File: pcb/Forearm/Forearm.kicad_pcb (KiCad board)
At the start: 4 copper layers, 64 x 64.1 mm, 22 parts, among them J1 Conn_01x02, J2 Conn_01x16_Top, J3 Conn_01x16_Bottom, J9 Conn_01x01, U1 ESP32-S3-DEVKITC-1-N8R2, U2 4754

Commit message: actually final pcbs
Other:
- board text added: "Dexterity Forearm JLL"
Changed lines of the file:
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@@
 		(property "Reference" "C1"
 			(at -3.253 0 180)
+			(unlocked yes)
 			(layer "F.SilkS")
 			(effects
 				(font
-					(size 1 1)
-					(thickness 0.15)
+					(size 1.016 1.016)
+					(thickness 0.1524)
 				)
 			)
@@
 		(property "Reference" "J9"
 			(at -0.0254 2.4892 0)
+			(unlocked yes)
 			(layer "F.SilkS")
 			(effects
 				(font
-					(size 1 1)
-					(thickness 0.15)
+					(size 1.016 1.016)
+					(thickness 0.1524)
 				)
 			)
@@
 		(property "Reference" "U1"
 			(at -14.224 -28.9032 0)
+			(unlocked yes)
 			(layer "F.SilkS")
 			(effects
 				(font
-					(size 1 1)
-					(thickness 0.15)
+					(size 1.016 1.016)
+					(thickness 0.1524)
 				)
 			)
@@
 		(property "Reference" "VR1"
 			(at -6.604 -2.032 -90)
+			(unlocked yes)
 			(layer "F.SilkS")
 			(effects
 				(font
-					(size 1.4 1.4)
-					(thickness 0.15)
+					(size 1.016 1.016)
+					(thickness 0.1524)
 				)
 			)
@@
 		(property "Reference" "REF**"
 			(at 0 -3.2 0)
+			(unlocked yes)
 			(layer "F.SilkS")
 			(hide yes)
 			(effects
 				(font
-					(size 1 1)
-					(thickness 0.15)
+					(size 1.016 1.016)
+					(thickness 0.1524)
 				)
 			)
@@
 		(property "Reference" "J1"
 			(at 0 -2.77 90)
+			(unlocked yes)
 			(layer "F.SilkS")
 			(effects
 				(font
-					(size 1 1)
-					(thickness 0.15)
+					(size 1.016 1.016)
+					(thickness 0.1524)
 				)
 			)
@@
 		(property "Reference" "U2"
 			(at 12.319 -12.573 0)
+			(unlocked yes)
 			(layer "F.SilkS")
 			(effects
 				(font
-					(size 1 1)
-					(thickness 0.15)
+					(size 1.016 1.016)
+					(thickness 0.1524)
 				)
 			)
@@
 		(property "Reference" "C2"
 			(at -3.302 0 180)
+			(unlocked yes)
 			(layer "F.SilkS")
 			(effects
 				(font
-					(size 1 1)
-					(thickness 0.15)
+					(size 1.016 1.016)
+					(thickness 0.1524)
 				)
 			)
@@
 		(property "Reference" "REF**"
 			(at 0 -3.2 0)
+			(unlocked yes)
 			(layer "F.SilkS")
 			(hide yes)
 			(effects
 				(font
-					(size 1 1)
-					(thickness 0.15)
+					(size 1.016 1.016)
+					(thickness 0.1524)
 				)
 			)
@@
 		(property "Reference" "REF**"
 			(at 0 -3.2 0)
+			(unlocked yes)
 			(layer "F.SilkS")
 			(hide yes)
 			(effects
 				(font
-					(size 1 1)
-					(thickness 0.15)
+					(size 1.016 1.016)
+					(thickness 0.1524)
 				)
 			)
@@
 		(tags "522071633 ")
 		(property "Reference" "J2"
-			(at 0 -7.62 180)
+			(at -0.547985 0.406001 180)
 			(unlocked yes)
 			(layer "F.SilkS")
 			(effects
 				(font
-					(size 1 1)
-					(thickness 0.15)
+					(size 1.016 1.016)
+					(thickness 0.1524)
 				)
 			)
@@
 			(at 0 -10.16 180)
 			(unlocked yes)
-			(layer "F.SilkS")
-			(effects
-				(font
-					(size 1 1)
-					(thickness 0.15)
-				)
-			)
-		)
-		(fp_text user "522071633"
-			(at 0 -10.16 180)
-			(unlocked yes)
 			(layer "F.Fab")
 			(effects
@@
 		(property "Reference" "RS0"
 			(at 0 1.17 90)
+			(unlocked yes)
 			(layer "B.SilkS")
 			(effects
 				(font
-					(size 1 1)
-					(thickness 0.15)
+					(size 1.016 1.016)
+					(thickness 0.1524)
 				)
 				(justify mirror)
@@
 		(property "Reference" "B0"
 			(at 0 2.77 90)
+			(unlocked yes)
 			(layer "B.SilkS")
 			(effects
 				(font
-					(size 1 1)
-					(thickness 0.15)
+					(size 1.016 1.016)
+					(thickness 0.1524)
 				)
 				(justify mirror)
@@
 		(property "Reference" "RLED0"
 			(at 0 1.17 0)
+			(unlocked yes)
 			(layer "B.SilkS")
 			(effects
 				(font
-					(size 1 1)
-					(thickness 0.15)
+					(size 1.016 1.016)
+					(thickness 0.1524)
 				)
 				(justify mirror)
@@
 		(property "Reference" "LED1"
 			(at 0 2.77 90)
+			(unlocked yes)
 			(layer "B.SilkS")
 			(effects
 				(font
-					(size 1 1)
-					(thickness 0.15)
+					(size 1.016 1.016)
+					(thickness 0.1524)
 				)
 				(justify mirror)
@@
 		(tags "522071633 ")
 		(property "Reference" "J3"
-			(at 0 7.62 180)
+			(at 0.293985 -0.406001 180)
 			(unlocked yes)
 			(layer "B.SilkS")
 			(effects
 				(font
-					(size 1 1)
-					(thickness 0.15)
+					(size 1.016 1.016)
+					(thickness 0.1524)
 				)
 				(justify mirror)
@@
 			(at 0 10.16 180)
 			(unlocked yes)
-			(layer "B.SilkS")
-			(effects
-				(font
-					(size 1 1)
-					(thickness 0.15)
-				)
-				(justify mirror)
-			)
-		)
-		(fp_text user "522071633"
-			(at 0 10.16 180)
-			(unlocked yes)
 			(layer "B.Fab")
 			(effects
@@
 		(property "Reference" "RB0"
 			(at 0 1.17 90)
+			(unlocked yes)
 			(layer "B.SilkS")
 			(effects
 				(font
-					(size 1 1)
-					(thickness 0.15)
+					(size 1.016 1.016)
+					(thickness 0.1524)
 				)
 				(justify mirror)
@@
 		(property "Reference" "LED0"
 			(at 0 2.77 90)
+			(unlocked yes)
 			(layer "B.SilkS")
 			(effects
 				(font
-					(size 1 1)
-					(thickness 0.15)
+					(size 1.016 1.016)
+					(thickness 0.1524)
 				)
 				(justify mirror)
@@
 		(property "Reference" "RLED1"
 			(at 0 1.17 0)
+			(unlocked yes)
 			(layer "B.SilkS")
 			(effects
 				(font
-					(size 1 1)
-					(thickness 0.15)
+					(size 1.016 1.016)
+					(thickness 0.1524)
 				)
 				(justify mirror)
@@
 		(property "Reference" "S0"
 			(at 0 2.77 90)
+			(unlocked yes)
 			(layer "B.SilkS")
 			(effects
 				(font
-					(size 1 1)
-					(thickness 0.15)
+					(size 1.016 1.016)
+					(thickness 0.1524)
 				)
 				(justify mirror)
@@
 		(property "Reference" "RB1"
 			(at 0 1.17 90)
+			(unlocked yes)
 			(layer "B.SilkS")
 			(effects
 				(font
-					(size 1 1)
-					(thickness 0.15)
+					(size 1.016 1.016)
+					(thickness 0.1524)
 				)
 				(justify mirror)
@@
 		(property "Reference" "B1"
 			(at 0 2.77 90)
+			(unlocked yes)
 			(layer "B.SilkS")
 			(effects
 				(font
-					(size 1 1)
-					(thickness 0.15)
+					(size 1.016 1.016)
+					(thickness 0.1524)
 				)
 				(justify mirror)
@@
 		(layer "Edge.Cuts")
 	)
+	(gr_text "Dexterity\nForearm\nJLL"
+		(at 21.7536 81.3928 0)
+		(layer "F.SilkS")
+		(effects
+			(font
+				(size 1.016 1.016)
+				(thickness 0.1524)
+			)
+			(justify bottom)
+		)
+	)
 	(segment

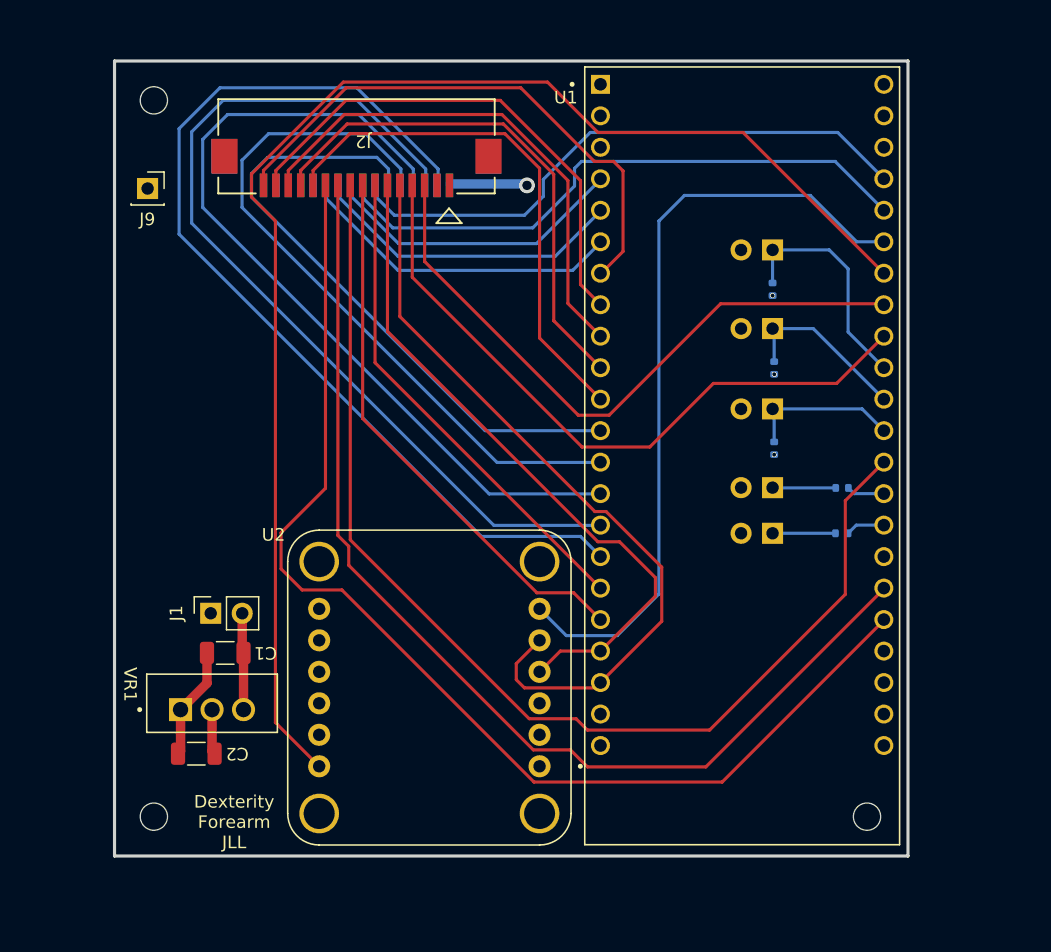
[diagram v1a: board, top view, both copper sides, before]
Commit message: added ground pours and generated gerbers for pcbs
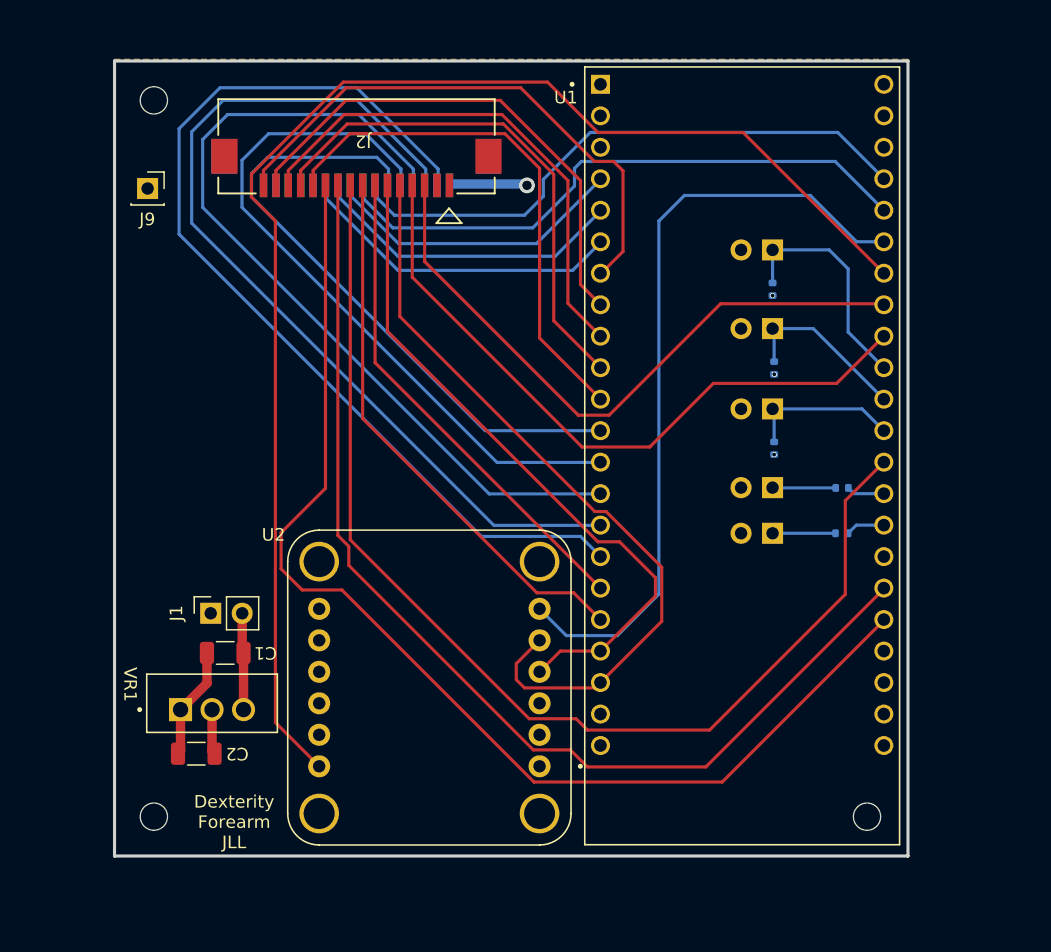
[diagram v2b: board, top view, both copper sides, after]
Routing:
- added copper zone on B.Cu, net GND
- added copper zone on F.Cu, net GND
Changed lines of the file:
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@@
 		(grid_origin 12.1016 81.9008)
 		(pcbplotparams
-			(layerselection 0x00010f0_ffffffff)
+			(layerselection 0x00010fc_ffffffff)
 			(plot_on_all_layers_selection 0x0000000_00000000)
 			(disableapertmacros no)
-			(usegerberextensions no)
-			(usegerberattributes yes)
-			(usegerberadvancedattributes yes)
-			(creategerberjobfile yes)
+			(usegerberextensions yes)
+			(usegerberattributes no)
+			(usegerberadvancedattributes no)
+			(creategerberjobfile no)
 			(dashed_line_dash_ratio 12.000000)
 			(dashed_line_gap_ratio 3.000000)
@@
 			(plotinvisibletext no)
 			(sketchpadsonfab no)
-			(subtractmaskfromsilk no)
+			(subtractmaskfromsilk yes)
 			(outputformat 1)
 			(mirror no)
@@
 	)
 	(zone
+		(net 1)
+		(net_name "GND")
+		(layer "F.Cu")
+		(hatch edge 0.5)
+		(priority 2)
+		(connect_pads
+			(clearance 0.5)
+		)
+		(min_thickness 0.25)
+		(filled_areas_thickness no)
+		(fill yes
+			(thermal_gap 0.5)
+			(thermal_bridge_width 0.5)
+		)
+		(polygon
+			(pts
+				(xy 12.1016 17.6388) (xy 76.1096 17.6388) (xy 76.1096 81.9008) (xy 12.1016 81.9008)
+			)
+		)
+	)
+	(zone
 		(net 3)
 		(net_name "3V3")
@@
 			)
 		)
+	)
+	(zone
+		(net 1)
+		(net_name "GND")
+		(layer "B.Cu")
+		(hatch edge 0.5)
+		(priority 3)
+		(connect_pads
+			(clearance 0.5)
+		)
+		(min_thickness 0.25)
+		(filled_areas_thickness no)
+		(fill yes
+			(thermal_gap 0.5)
+			(thermal_bridge_width 0.5)
+		)
+		(polygon
+			(pts
+				(xy 76.1096 17.6388) (xy 76.1096 81.9008) (xy 12.1016 81.9008) (xy 12.1016 17.6388)
+			)
+		)

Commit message: edited esp32 footprint
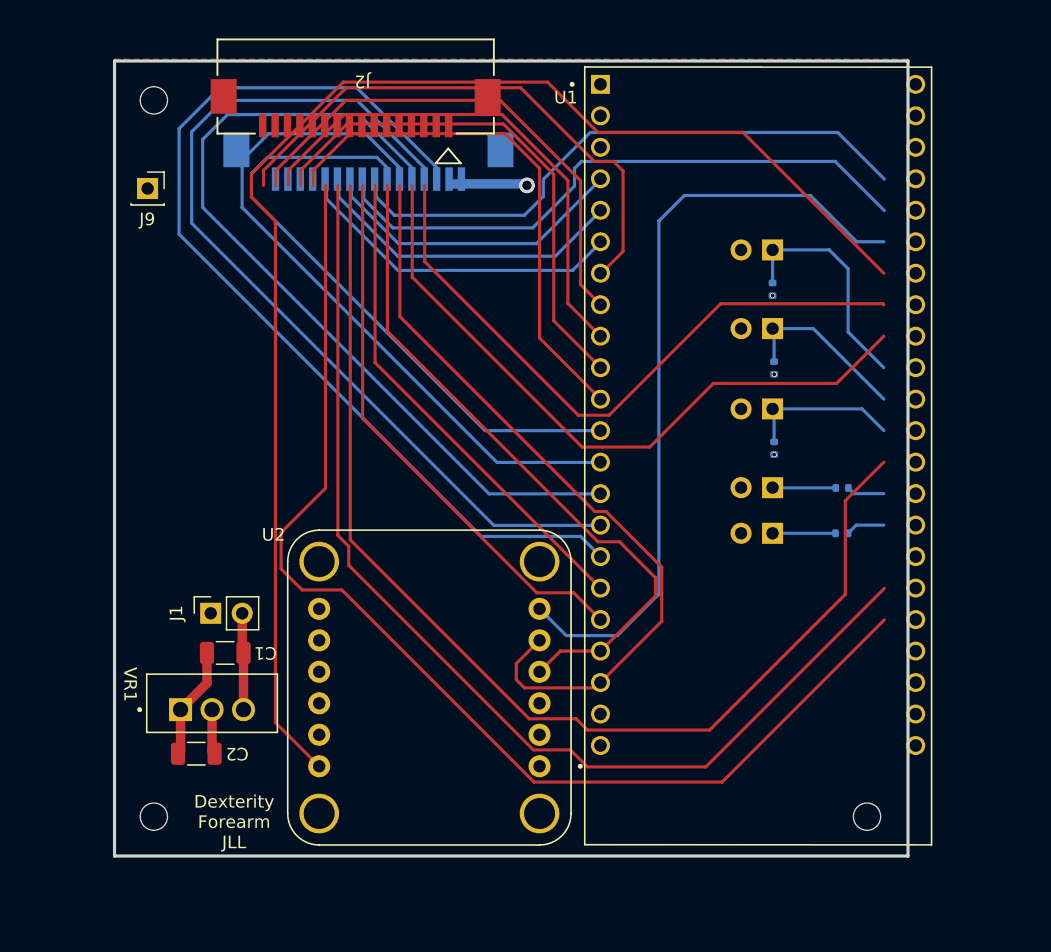
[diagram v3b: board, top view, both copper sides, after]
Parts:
- moved J2 4.83 mm to (31.6, 19.8)
- moved J3 1.09 mm to (32.6, 24.1)
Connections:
- J2 pad 1: unconnected-(J2-Pin_1-Pad1) -> FEEDBACK_D4
- J2 pad 10: HAPTIC_S1 -> HAPTIC_SCL
- J2 pad 11: HAPTIC_S0 -> IMU_SCL
- J2 pad 12: FEEDBACK_D0 -> IMU_SDA
- J2 pad 13: FEEDBACK_D1 -> IMU_1_RST
- J2 pad 14: FEEDBACK_D2 -> IMU_1_INT
- J2 pad 15: FEEDBACK_D3 -> unconnected-(J2-Pin_15-Pad15)
- J2 pad 16: FEEDBACK_D4 -> unconnected-(J2-Pin_16-Pad16)
- J2 pad 2: unconnected-(J2-Pin_2-Pad2) -> FEEDBACK_D3
- J2 pad 3: IMU_1_INT -> FEEDBACK_D2
- J2 pad 4: IMU_1_RST -> FEEDBACK_D1
- J2 pad 5: IMU_SDA -> FEEDBACK_D0
- J2 pad 6: IMU_SCL -> HAPTIC_S0
- J2 pad 7: HAPTIC_SCL -> HAPTIC_S1
- J2 pad 8: HAPTIC_SDA -> HAPTIC_S2
- J2 pad 9: HAPTIC_S2 -> HAPTIC_SDA
- J3 pad 1: unconnected-(J3-Pin_1-Pad1) -> 3V3
- J3 pad 10: SPOOLPOT_ADC0 -> SPOOLPOT_ADC3
- J3 pad 11: HALL_S3 -> SPOOLPOT_ADC4
- J3 pad 12: HALL_S2 -> GND
- J3 pad 13: HALL_S1 -> unconnected-(J3-Pin_13-Pad13)
- J3 pad 14: HALL_S0 -> unconnected-(J3-Pin_14-Pad14)
- J3 pad 15: HALL_ADC -> unconnected-(J3-Pin_15-Pad15)
- J3 pad 16: 3V3 -> unconnected-(J3-Pin_16-Pad16)
- J3 pad 2: unconnected-(J3-Pin_2-Pad2) -> HALL_ADC
- J3 pad 3: unconnected-(J3-Pin_3-Pad3) -> HALL_S0
- J3 pad 4: unconnected-(J3-Pin_4-Pad4) -> HALL_S1
- J3 pad 5: unconnected-(J3-Pin_5-Pad5) -> HALL_S2
- J3 pad 6: SPOOLPOT_ADC4 -> HALL_S3
- J3 pad 7: SPOOLPOT_ADC3 -> SPOOLPOT_ADC0
- J3 pad 8: SPOOLPOT_ADC2 -> SPOOLPOT_ADC1
- J3 pad 9: SPOOLPOT_ADC1 -> SPOOLPOT_ADC2
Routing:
- net SPOOLPOT_ADC2: track 24.9 -> 72.7 mm
- net SPOOLPOT_ADC0: track 47.8 -> 0.00 mm
- net unconnected-(J3-Pin_16-Pad16): track 0.00 -> 6.22 mm
- net 3V3: track 9.86 -> 3.64 mm

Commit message: updated esp32 pins on schematic
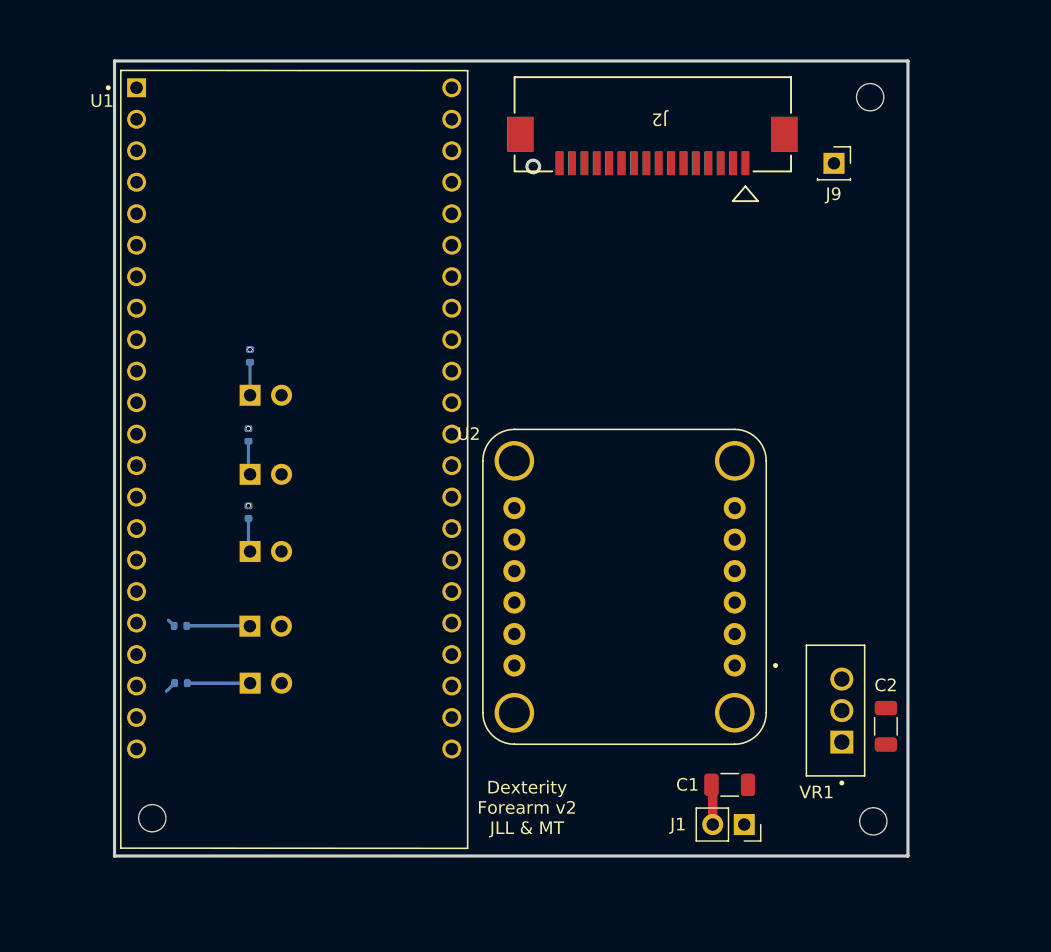
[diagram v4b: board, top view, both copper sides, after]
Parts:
- moved REF** 57.8 mm to (73.1, 20.7)
- moved C2 55.7 mm to (74.3, 71.4), turned to -90 degrees
- moved J9 55.4 mm to (70.1, 26.0)
- moved RLED1 54.7 mm to (17.5, 68.0), turned to 180 degrees
- moved RLED0 54.5 mm to (17.4, 63.3), turned to 180 degrees
- moved VR1 50.8 mm to (70.8, 70.2), turned to 90 degrees
- moved J1 46.3 mm to (62.9, 79.4), turned to -90 degrees
- moved LED1 43.8 mm to (23.0, 68.0), turned to -90 degrees
- moved B0 43.8 mm to (23.0, 51.1), turned to -90 degrees
- moved S0 43.8 mm to (23.0, 44.7), turned to -90 degrees
- moved B1 43.7 mm to (23.0, 57.3), turned to -90 degrees
- moved LED0 43.6 mm to (23.0, 63.4), turned to -90 degrees
- moved RB0 42.7 mm to (22.9, 47.9), turned to 90 degrees
- moved RB1 42.7 mm to (22.9, 54.2), turned to 90 degrees
- moved RS0 42.5 mm to (23.0, 41.6), turned to 90 degrees
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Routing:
- net IMU_0_RST: track 110.5 -> 0.00 mm
- net HAPTIC_S0: track 93.6 -> 0.00 mm
- net HAPTIC_S2: track 91.4 -> 0.00 mm
- net HAPTIC_S1: track 86.9 -> 0.00 mm
- net HALL_ADC: track 79.5 -> 0.00 mm
- net HALL_S0: track 73.9 -> 0.00 mm
- net SPOOLPOT_ADC2: track 72.7 -> 0.00 mm
- net HALL_S1: track 68.0 -> 0.00 mm
- net IMU_SDA: track 63.2 -> 0.00 mm
- net IMU_0_INT: track 63.1 -> 0.00 mm
- net HALL_S2: track 57.4 -> 0.00 mm
- net IMU_SCL: track 55.5 -> 0.00 mm
- net IMU_1_RST: track 54.8 -> 0.00 mm
- net IMU_1_INT: track 52.1 -> 0.00 mm
- net HALL_S3: track 51.0 -> 0.00 mm
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- removed copper zone on B.Cu, net GND
- removed copper zone on F.Cu, net GND
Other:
- board text added: "Dexterity Forearm v2 JLL & MT"
- board text removed: "Dexterity Forearm JLL"

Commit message: board done will upload to JCL to check for errors
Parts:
- moved J9 11.3 mm to (59.9, 30.7)
- moved REF** 0.28 mm to (73.3, 20.6)
- moved REF** 0.28 mm to (15.0, 79.1)
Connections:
- J2 pad 13: IMU_1_RST -> IMU_RST
- U1 pad J1_10: FEEDBACK_D1 -> FEEDBACK_D3
- U1 pad J1_11: FEEDBACK_D0 -> FEEDBACK_D2
- U1 pad J1_12: HALL_S3 -> FEEDBACK_D1
- U1 pad J1_13: HALL_S2 -> FEEDBACK_D0
- U1 pad J1_14: HALL_S1 -> unconnected-(U1-GPIO46-PadJ1_14)
- U1 pad J1_15: HALL_S0 -> SWITCH_0
- U1 pad J1_16: HALL_ADC -> BUTTON_0
- U1 pad J1_17: HAPTIC_SCL -> BUTTON_1
- U1 pad J1_18: HAPTIC_SDA -> LED_0
- U1 pad J1_19: IMU_SCL -> LED_1
- U1 pad J1_20: IMU_SDA -> IMU_0_INT
- U1 pad J1_4: SPOOLPOT_ADC2 -> SPOOLPOT_ADC4
- U1 pad J1_6: SPOOLPOT_ADC4 -> SPOOLPOT_ADC2
- U1 pad J1_7: FEEDBACK_D4 -> SPOOLPOT_ADC0
- U1 pad J1_8: FEEDBACK_D3 -> SPOOLPOT_ADC1
- U1 pad J1_9: FEEDBACK_D2 -> FEEDBACK_D4
- U1 pad J3_10: SWITCH_0 -> IMU_RST
- U1 pad J3_11: BUTTON_0 -> IMU_SDA
- U1 pad J3_12: BUTTON_1 -> IMU_SCL
- U1 pad J3_13: HAPTIC_S2 -> HAPTIC_SCL
- U1 pad J3_14: LED_0 -> HAPTIC_SDA
- U1 pad J3_15: LED_1 -> HAPTIC_S2
- U1 pad J3_4: SPOOLPOT_ADC0 -> HALL_ADC
- U1 pad J3_5: SPOOLPOT_ADC1 -> HALL_S0
- U1 pad J3_6: IMU_0_INT -> HALL_S1
- U1 pad J3_7: IMU_0_RST -> HALL_S2
- U1 pad J3_8: IMU_1_INT -> HALL_S3
- U1 pad J3_9: IMU_1_RST -> IMU_1_INT
- U2 pad JP2_1: IMU_0_RST -> IMU_RST
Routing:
- net IMU_0_INT: track 0.00 -> 73.1 mm
- net FEEDBACK_D4: track 0.00 -> 62.0 mm
- net FEEDBACK_D3: track 0.00 -> 61.7 mm
- net FEEDBACK_D0: track 0.00 -> 60.4 mm
- net FEEDBACK_D2: track 0.00 -> 59.8 mm
- net FEEDBACK_D1: track 0.00 -> 59.4 mm
- net IMU_SCL: track 0.00 -> 54.9 mm
- net IMU_SDA: track 0.00 -> 52.0 mm
- net SPOOLPOT_ADC4: track 0.00 -> 51.9 mm
- net IMU_RST: track 0.00 -> 50.4 mm
- net SPOOLPOT_ADC1: track 0.00 -> 50.1 mm
- net SPOOLPOT_ADC3: track 0.00 -> 49.6 mm
- net SPOOLPOT_ADC2: track 0.00 -> 48.7 mm
- net SPOOLPOT_ADC0: track 0.00 -> 47.9 mm
- net HAPTIC_S0: track 0.00 -> 46.3 mm
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- added copper zone on B.Cu, net GND
- added copper zone on F.Cu, net GND
